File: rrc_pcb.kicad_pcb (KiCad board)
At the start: 2 copper layers, 147.3 x 56.3 mm, 20 parts, among them J1 Voltage Regulator Input, J2 Conn_01x03_Male, U1 ADXL357Z, U2 Teensy3.6-teensy, U3 BN220-GPS, U4 MS5611, U5 logo

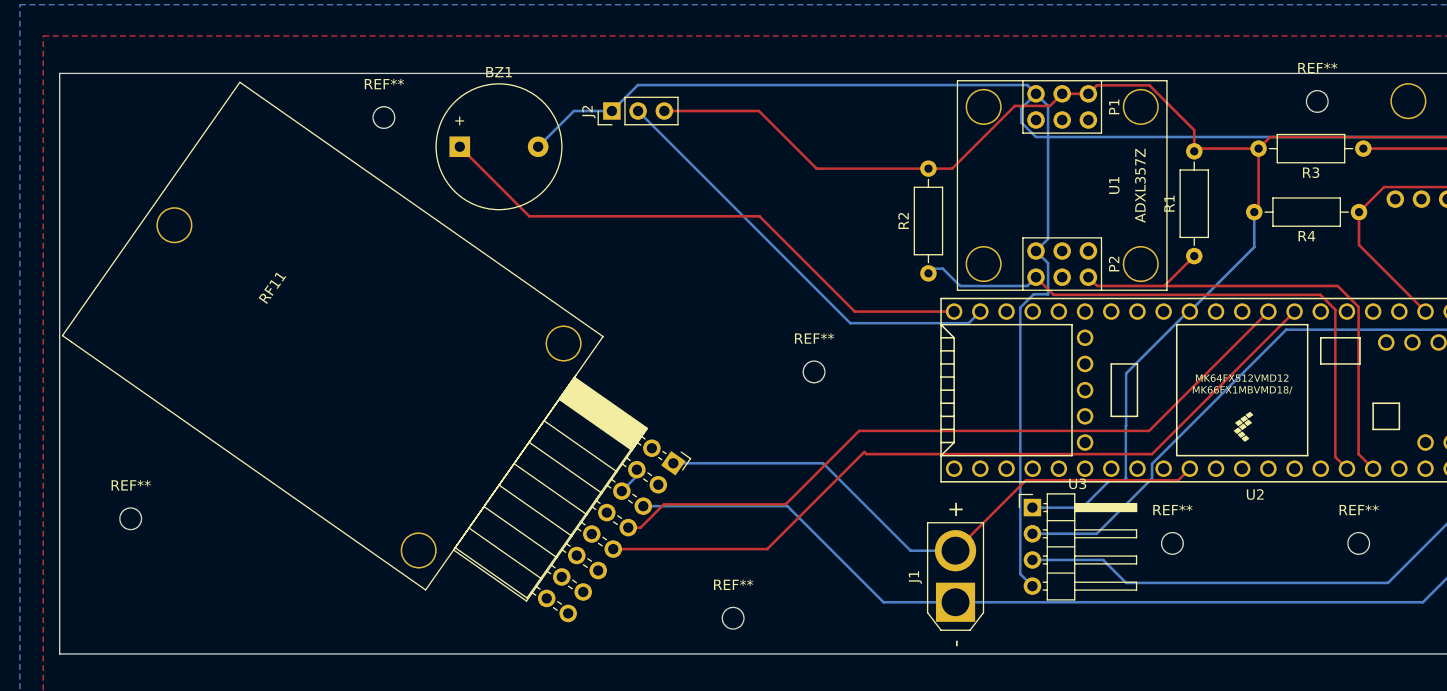
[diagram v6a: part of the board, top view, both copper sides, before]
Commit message: reoriented rfd
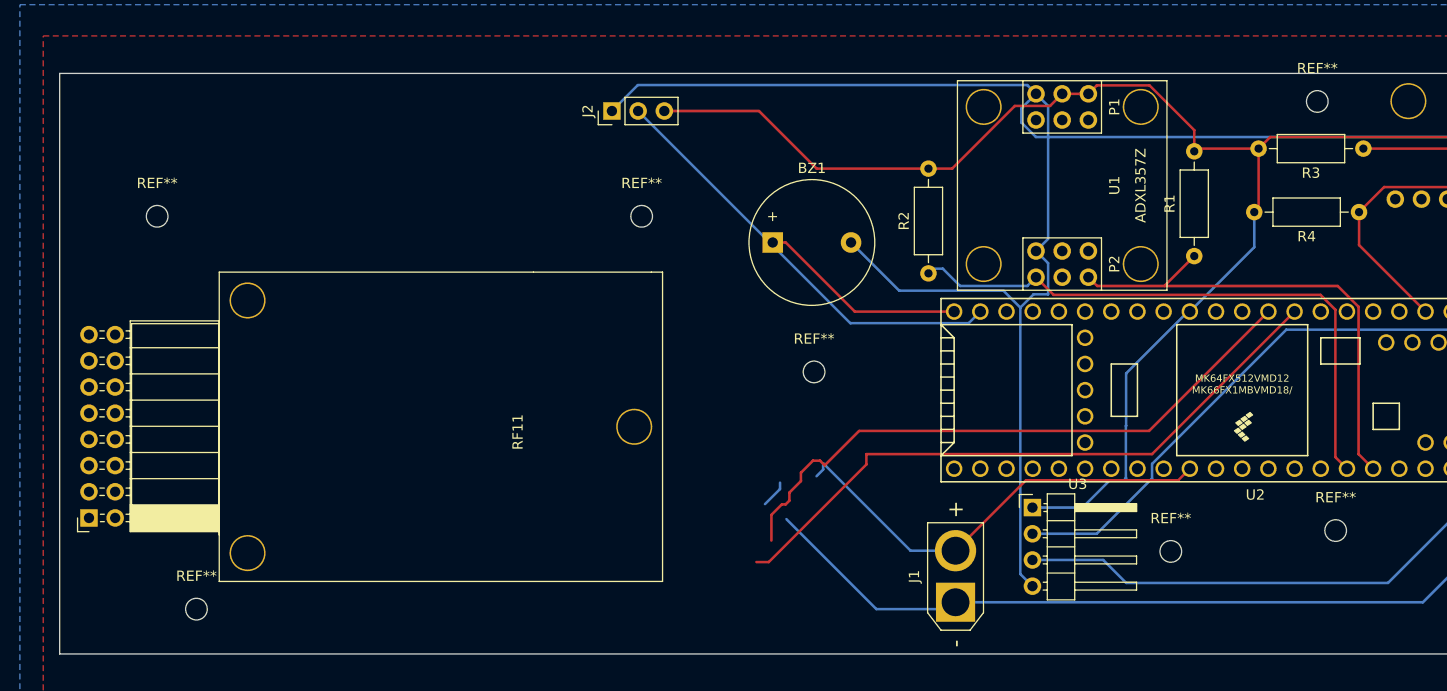
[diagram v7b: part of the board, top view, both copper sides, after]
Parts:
- moved REF** 57.6 mm to (74.9, 35.6)
- moved REF** 52.1 mm to (31.8, 73.7)
- moved RF11 36.8 mm to (34.0, 41.0), turned to -90 degrees
- moved BZ1 31.7 mm to (87.6, 38.1)
- moved REF** 24.0 mm to (27.9, 35.6)
- moved U5 15.5 mm to (54.6, 35.6), turned to 180 degrees
- moved REF** 2.56 mm to (142.2, 66.0)
- moved REF** 0.79 mm to (126.3, 68.1)
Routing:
- net Net-(BZ1-Pad1): track 54.6 -> 20.4 mm
- net VCC: track 97.8 -> 83.9 mm
- net GND: track 56.9 -> 43.9 mm
- net Net-(RF11-Pad9): track 75.8 -> 62.8 mm
- net Net-(RF11-Pad7): track 70.8 -> 60.2 mm
- net T_GND: track 170.3 -> 180.7 mm

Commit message: buzzer fix
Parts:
- moved BZ1 54.1 mm to (34.3, 29.2)
- moved REF** 5.24 mm to (26.7, 74.9)
- moved RF11 2.39 mm to (33.4, 43.3)
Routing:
- net Net-(RF11-Pad9): track 62.8 -> 144.9 mm
- net VCC: track 83.9 -> 159.3 mm, vias 0 -> 1
- net GND: track 43.9 -> 117.6 mm
- net Net-(RF11-Pad7): track 60.2 -> 123.1 mm
- net Net-(BZ1-Pad1): track 20.4 -> 77.4 mm
- net T_GND: track 180.7 -> 193.4 mm
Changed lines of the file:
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@@
   )
   (footprint "rfd900+:RFD900+" (layer "F.Cu")
-    (at 33.95844 40.975 -90)
+    (at 33.409172 43.297943 -90)
     (property "Sheetfile" "D:/Alessandro/FILESFORSCHOOL/RRC-Avionics-master/PCB design/PCB/rrc_pcb.sch")
     (property "Sheetname" "")
@@
   )
   (footprint "Buzzer_Beeper:Buzzer_12x9.5RM7.6" (layer "F.Cu")
-    (at 87.64 38.1)
+    (at 34.3 29.21)
     (descr "Generic Buzzer, D12mm height 9.5mm with RM7.6mm")
     (tags "buzzer")
@@
   )
   (footprint "MountingHole:MountingHole_2.1mm" (layer "F.Cu")
-    (at 31.75 73.66)
+    (at 26.67 74.93)
     (descr "Mounting Hole 2.1mm, no annular")
     (tags "mounting hole 2.1mm no annular")
@@
   (segment (start 105.373647 67.993284) (end 112.200514 61.166417) (width 0.25) (layer "F.Cu") (net 1))
   (segment (start 112.200514 61.166417) (end 126.972999 61.166417) (width 0.25) (layer "F.Cu") (net 1))
+  (segment (start 22.142781 65.774714) (end 20.777292 67.140203) (width 0.25) (layer "B.Cu") (net 1))
+  (segment (start 92.533994 59.513994) (end 92.533994 60.123915) (width 0.25) (layer "B.Cu") (net 1))
+  (segment (start 26.935286 65.774714) (end 22.142781 65.774714) (width 0.25) (layer "B.Cu") (net 1))
+  (segment (start 91.887208 60.770701) (end 31.939299 60.770701) (width 0.25) (layer "B.Cu") (net 1))
+  (segment (start 92.533994 60.123915) (end 91.887208 60.770701) (width 0.25) (layer "B.Cu") (net 1))
+  (segment (start 105.373647 67.993284) (end 101.013284 67.993284) (width 0.25) (layer "B.Cu") (net 1))
+  (segment (start 31.939299 60.770701) (end 26.935286 65.774714) (width 0.25) (layer "B.Cu") (net 1))
   (segment (start 101.013284 67.993284) (end 92.533994 59.513994) (width 0.25) (layer "B.Cu") (net 1))
-  (segment (start 105.373647 67.993284) (end 101.013284 67.993284) (width 0.25) (layer "B.Cu") (net 1))
-  (segment (start 91.887208 60.770701) (end 92.533994 60.123915) (width 0.25) (layer "B.Cu") (net 1))
-  (segment (start 92.533994 60.123915) (end 92.533994 59.513994) (width 0.25) (layer "B.Cu") (net 1))
+  (segment (start 22.830793 63.234714) (end 30.214714 63.234714) (width 0.25) (layer "F.Cu") (net 2))
+  (segment (start 30.214714 63.234714) (end 30.48 63.5) (width 0.25) (layer "F.Cu") (net 2))
+  (segment (start 21.656282 62.060203) (end 22.830793 63.234714) (width 0.25) (layer "F.Cu") (net 2))
+  (segment (start 20.777292 62.060203) (end 21.656282 62.060203) (width 0.25) (layer "F.Cu") (net 2))
+  (segment (start 30.48 63.5) (end 35.56 63.5) (width 0.25) (layer "F.Cu") (net 2))
+  (via (at 35.56 63.5) (size 0.8) (drill 0.4) (layers "F.Cu" "B.Cu") (net 2))
+  (segment (start 88.97344 64.931993) (end 85.590719 68.314714) (width 0.25) (layer "B.Cu") (net 2))
   (segment (start 104.14 73.66) (end 97.701447 73.66) (width 0.25) (layer "B.Cu") (net 2))
+  (segment (start 35.294714 63.765286) (end 35.56 63.5) (width 0.25) (layer "B.Cu") (net 2))
   (segment (start 97.701447 73.66) (end 88.97344 64.931993) (width 0.25) (layer "B.Cu") (net 2))
   (segment (start 104.806716 72.993284) (end 104.14 73.66) (width 0.25) (layer "B.Cu") (net 2))
+  (segment (start 35.294714 68.314714) (end 35.294714 63.765286) (width 0.25) (layer "B.Cu") (net 2))
   (segment (start 150.706132 72.993284) (end 163.65751 60.041906) (width 0.25) (layer "B.Cu") (net 2))
   (segment (start 105.373647 72.993284) (end 104.806716 72.993284) (width 0.25) (layer "B.Cu") (net 2))
   (segment (start 105.373647 72.993284) (end 150.706132 72.993284) (width 0.25) (layer "B.Cu") (net 2))
+  (segment (start 85.590719 68.314714) (end 35.294714 68.314714) (width 0.25) (layer "B.Cu") (net 2))
   (segment (start 111.127794 24.855912) (end 105.046864 30.936842) (width 0.25) (layer "F.Cu") (net 3))
   (segment (start 128.790528 28.995101) (end 128.526625 29.259004) (width 0.25) (layer "F.Cu") (net 3))
@@
   (segment (start 146.938937 32.721917) (end 144.506564 35.15429) (width 0.25) (layer "F.Cu") (net 7))
   (segment (start 154.471553 32.721917) (end 146.938937 32.721917) (width 0.25) (layer "F.Cu") (net 7))
-  (segment (start 90.378869 61.241792) (end 90.378869 60.427542) (width 0.25) (layer "F.Cu") (net 11))
   (segment (start 124.142021 56.377395) (end 135.71751 44.801906) (width 0.25) (layer "F.Cu") (net 11))
-  (segment (start 88.528912 63.5) (end 88.9 63.5) (width 0.25) (layer "F.Cu") (net 11))
+  (segment (start 21.951803 58.345692) (end 20.777292 59.520203) (width 0.25) (layer "F.Cu") (net 11))
+  (segment (start 90.323781 60.372454) (end 55.292454 60.372454) (width 0.25) (layer "F.Cu") (net 11))
+  (segment (start 90.378869 60.427542) (end 90.323781 60.372454) (width 0.25) (layer "F.Cu") (net 11))
   (segment (start 90.378869 60.427542) (end 91.544049 59.262362) (width 0.25) (layer "F.Cu") (net 11))
-  (segment (start 89.255813 63.144187) (end 89.255813 62.364848) (width 0.25) (layer "F.Cu") (net 11))
-  (segment (start 87.516555 67.012639) (end 87.516555 64.512357) (width 0.25) (layer "F.Cu") (net 11))
-  (segment (start 87.516555 64.512357) (end 88.528912 63.5) (width 0.25) (layer "F.Cu") (net 11))
+  (segment (start 25.4 58.42) (end 25.325692 58.345692) (width 0.25) (layer "F.Cu") (net 11))
+  (segment (start 55.292454 60.372454) (end 53.34 58.42) (width 0.25) (layer "F.Cu") (net 11))
   (segment (start 96.022605 56.377395) (end 124.142021 56.377395) (width 0.25) (layer "F.Cu") (net 11))
-  (segment (start 88.9 63.5) (end 89.255813 63.144187) (width 0.25) (layer "F.Cu") (net 11))
+  (segment (start 53.34 58.42) (end 25.4 58.42) (width 0.25) (layer "F.Cu") (net 11))
   (segment (start 92.684003 59.715997) (end 96.022605 56.377395) (width 0.25) (layer "F.Cu") (net 11))
-  (segment (start 89.255813 62.364848) (end 90.378869 61.241792) (width 0.25) (layer "F.Cu") (net 11))
   (segment (start 92.230367 59.262362) (end 92.684003 59.715997) (width 0.25) (layer "F.Cu") (net 11))
+  (segment (start 25.325692 58.345692) (end 21.951803 58.345692) (width 0.25) (layer "F.Cu") (net 11))
   (segment (start 91.544049 59.262362) (end 92.230367 59.262362) (width 0.25) (layer "F.Cu") (net 11))
-  (segment (start 88.349678 62.018224) (end 88.349678 61.394463) (width 0.25) (layer "B.Cu") (net 12))
-  (segment (start 86.892793 63.475109) (end 88.349678 62.018224) (width 0.25) (layer "B.Cu") (net 12))
+  (segment (start 23.317292 62.060203) (end 23.317292 64.600203) (width 0.25) (layer "B.Cu") (net 12))
+  (segment (start 19.602781 69.132781) (end 23.092454 72.622454) (width 0.25) (layer "F.Cu") (net 14))
+  (segment (start 19.602781 58.154714) (end 19.602781 69.132781) (width 0.25) (layer "F.Cu") (net 14))
+  (segment (start 82.530502 72.622454) (end 86.059671 69.093285) (width 0.25) (layer "F.Cu") (net 14))
   (segment (start 86.059671 69.093285) (end 87.261752 69.093285) (width 0.25) (layer "F.Cu") (net 14))
   (segment (start 96.726417 58.626417) (end 124.432999 58.626417) (width 0.25) (layer "F.Cu") (net 14))
@@
   (segment (start 87.261752 69.093285) (end 96.726417 59.62862) (width 0.25) (layer "F.Cu") (net 14))
   (segment (start 96.726417 59.62862) (end 96.726417 58.626417) (width 0.25) (layer "F.Cu") (net 14))
-  (segment (start 110.016081 42.768921) (end 99.908921 42.768921) (width 0.25) (layer "B.Cu") (net 22))
-  (segment (start 111.658138 44.410978) (end 110.016081 42.768921) (width 0.25) (layer "B.Cu") (net 22))
+  (segment (start 23.092454 72.622454) (end 82.530502 72.622454) (width 0.25) (layer "F.Cu") (net 14))
+  (segment (start 20.777292 56.980203) (end 19.602781 58.154714) (width 0.25) (layer "F.Cu") (net 14))
+  (segment (start 72.046305 25.348094) (end 45.761906 25.348094) (width 0.25) (layer "B.Cu") (net 22))
   (segment (start 114.353013 37.75489) (end 113.178502 38.929401) (width 0.25) (layer "B.Cu") (net 22))
+  (segment (start 45.761906 25.348094) (end 41.9 29.21) (width 0.25) (layer "B.Cu") (net 22))
   (segment (start 74.562998 22.831401) (end 112.328502 22.831401) (width 0.25) (layer "B.Cu") (net 22))
   (segment (start 160.726064 33.896428) (end 154.700226 27.87059) (width 0.25) (layer "B.Cu") (net 22))
@@
   (segment (start 111.76 26.463909) (end 111.76 25.099903) (width 0.25) (layer "B.Cu") (net 22))
   (segment (start 113.178502 23.681401) (end 114.353013 24.855912) (width 0.25) (layer "B.Cu") (net 22))
-  (segment (start 99.908921 42.768921) (end 95.24 38.1) (width 0.25) (layer "B.Cu") (net 22))
   (segment (start 111.76 25.099903) (end 113.178502 23.681401) (width 0.25) (layer "B.Cu") (net 22))
   (segment (start 112.328502 22.831401) (end 113.178502 23.681401) (width 0.25) (layer "B.Cu") (net 22))
@@
   (segment (start 156.822368 46.557048) (end 158.57751 44.801906) (width 0.25) (layer "B.Cu") (net 44))
   (segment (start 119.067843 66.352157) (end 124.432999 60.987001) (width 0.25) (layer "B.Cu") (net 44))
-  (segment (start 88.9 38.1) (end 87.64 38.1) (width 0.25) (layer "F.Cu") (net 74))
+  (segment (start 43.19 38.1) (end 88.9 38.1) (width 0.25) (layer "F.Cu") (net 74))
   (segment (start 95.601906 44.801906) (end 105.23751 44.801906) (width 0.25) (layer "F.Cu") (net 74))
+  (segment (start 34.3 29.21) (end 43.19 38.1) (width 0.25) (layer "F.Cu") (net 74))
   (segment (start 88.9 38.1) (end 95.601906 44.801906) (width 0.25) (layer "F.Cu") (net 74))
   (segment (start 106.652999 45.926417) (end 107.77751 44.801906) (width 0.25) (layer "B.Cu") (net 75))
